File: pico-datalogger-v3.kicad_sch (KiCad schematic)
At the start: 38 parts, among them IC1 LM66200DRLR, J1 JST-PH2 Bat, J11 Conn_I2C1, J12 Conn_UART_5V, J13 THT_I2C1, J14 THT_I2C0, J17 Disp_THT, J2 Conn_Pico_Left, J3 Conn_Pico_Right, J4 SM06B-GHS-TB_LF_SN, J6 Conn_Display, J9 Conn_I2C0, Q1 AO3401A, Q2 AO3401A, U1 74LVC2G74, U2 PCF8523T, U3 Pico, U4 XTSD, Y1 Crystal

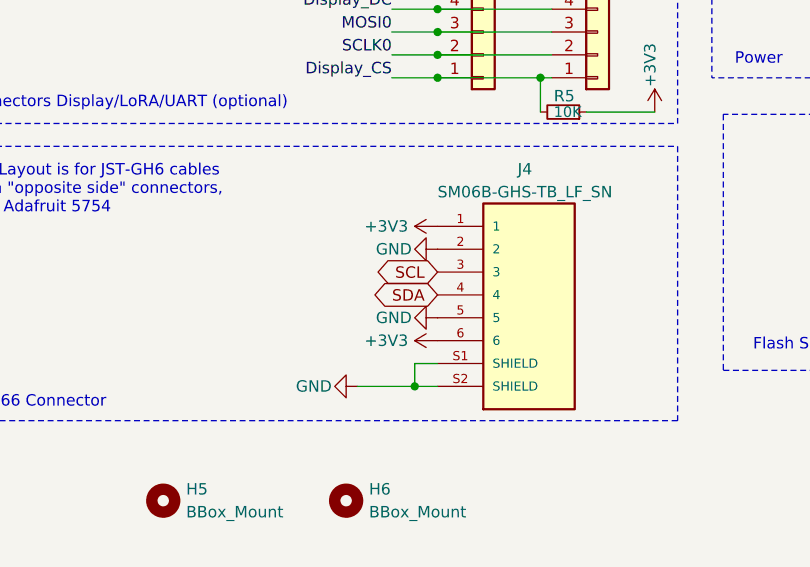
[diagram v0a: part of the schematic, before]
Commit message: updated production-files for datalogger-v3 and images
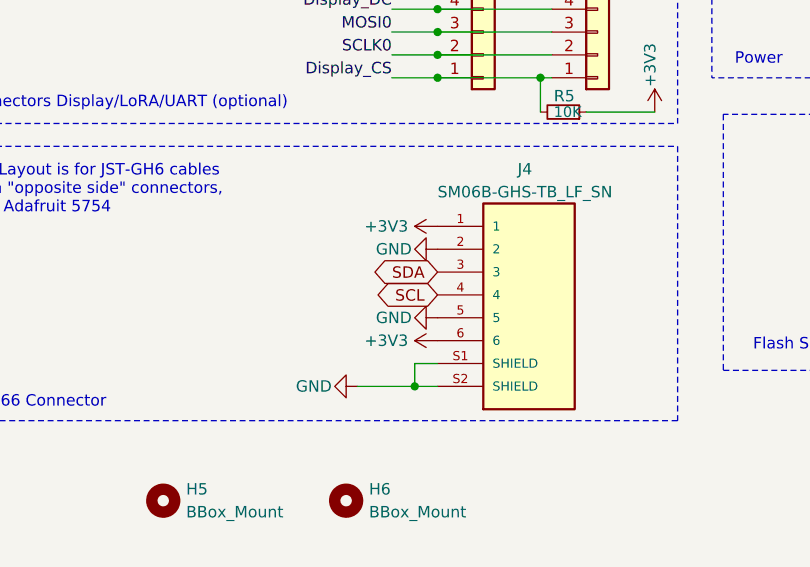
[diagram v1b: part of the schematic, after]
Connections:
- net SCL: now also J4.4; no longer J4.3
- net SDA: now also J4.3; no longer J4.4
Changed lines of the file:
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@@
   (title_block
     (title "pico-datalogger-v3")
-    (date "2025-11-21")
-    (rev "3.00")
+    (date "2025-12-29")
+    (rev "3.01")
     (company "Bernhard Bablok")
     (comment 1 "https://github.com/bablokb/pcb-pico-datalogger")
@@
     )
   )
-  (global_label "SDA" (shape bidirectional) (at 168.91 151.13 180) (fields_autoplaced)
-    (effects (font (size 1.27 1.27)) (justify right))
-    (property "Intersheetrefs" "${INTERSHEET_REFS}" (at 162.0584 151.13 0)
+  (global_label "SDA" (shape bidirectional) (at 168.91 148.59 180) (fields_autoplaced)
+    (effects (font (size 1.27 1.27)) (justify right))
+    (property "Intersheetrefs" "${INTERSHEET_REFS}" (at 162.0584 148.59 0)
       (effects (font (size 1.27 1.27)) (justify right) hide)
     )
@@
     )
   )
-  (global_label "SCL" (shape bidirectional) (at 168.91 148.59 180) (fields_autoplaced)
-    (effects (font (size 1.27 1.27)) (justify right))
-    (property "Intersheetrefs" "${INTERSHEET_REFS}" (at 162.1189 148.59 0)
+  (global_label "SCL" (shape bidirectional) (at 168.91 151.13 180) (fields_autoplaced)
+    (effects (font (size 1.27 1.27)) (justify right))
+    (property "Intersheetrefs" "${INTERSHEET_REFS}" (at 162.1189 151.13 0)
       (effects (font (size 1.27 1.27)) (justify right) hide)
     )

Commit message: Rev. 3.10: use XSON-8 package for flip-flop
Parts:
- U1: footprint Package_SO:TSSOP-8_3x3mm_P0.65mm -> Package_SON:X2SON-8_1.4x1mm_P0.35mm; LCSC C282355 -> C548678
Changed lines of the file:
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@@
   (title_block
     (title "pico-datalogger-v3")
-    (date "2026-01-15")
-    (rev "3.02")
+    (date "2026-02-19")
+    (rev "3.10")
     (company "Bernhard Bablok")
     (comment 1 "https://github.com/bablokb/pcb-pico-datalogger")
@@
       (effects (font (size 1.524 1.524)) (justify left))
     )
-    (property "Footprint" "Package_SO:TSSOP-8_3x3mm_P0.65mm" (at 251.46 50.8 0)
+    (property "Footprint" "Package_SON:X2SON-8_1.4x1mm_P0.35mm" (at 251.46 50.8 0)
       (effects (font (size 1.27 1.27)) hide)
     )
@@
       (effects (font (size 1.524 1.524)) (justify left) hide)
     )
-    (property "LCSC" "C282355" (at 251.46 49.53 0)
+    (property "LCSC" "C548678" (at 251.46 49.53 0)
       (effects (font (size 1.27 1.27)) hide)
     )
